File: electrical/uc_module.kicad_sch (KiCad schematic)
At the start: 10 parts, among them J6 Conn_01x06_Pin, SW2 SW_SPST, U1 ATtiny84A-PU

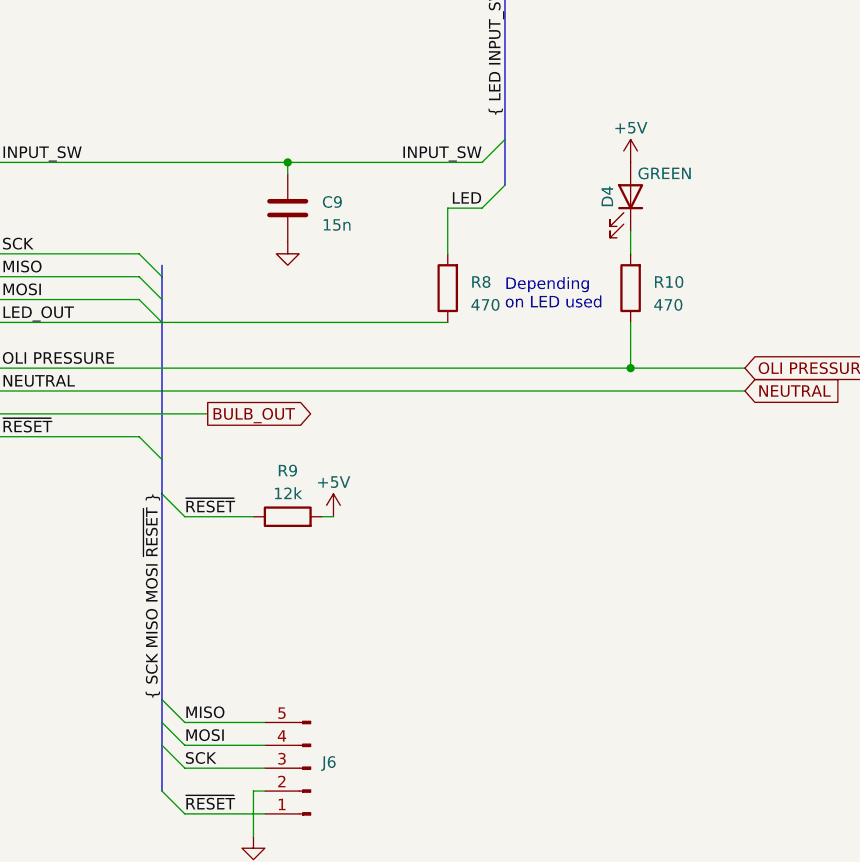
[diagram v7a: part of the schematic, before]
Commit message: Aktualizacja KiCad i schematu - LED do debugowania
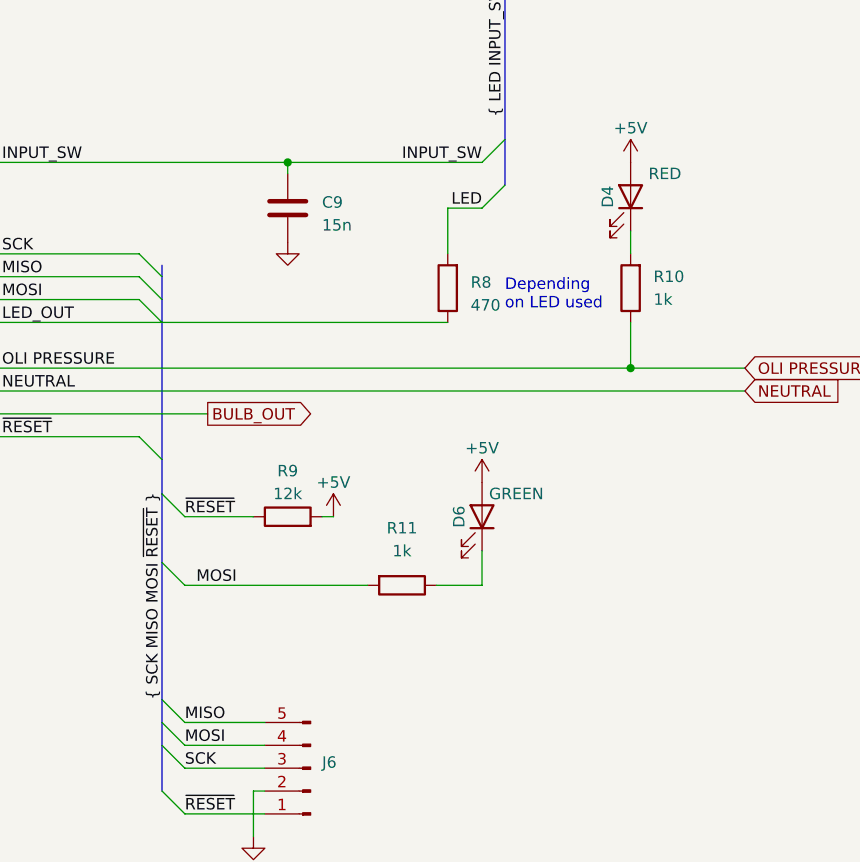
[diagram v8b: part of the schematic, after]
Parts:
- added D6: GREEN, symbol Device:LED
- added R11: 1k, symbol Device:R
- D4: value GREEN -> RED
- R10: value 470 -> 1k
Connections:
- net +5V: now also D6.2 (A)
- net MOSI: now also R11.2
- new net: D6.1 (K), R11.1
